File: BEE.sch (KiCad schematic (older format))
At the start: 74 parts, among them J1 RPI1_header, J10 Conn_01x02, J11 Conn_01x02, J12 Conn_01x02, J13 Conn_01x06, J14 Conn_01x03, J15 Conn_02x10_Odd_Even, J16 Conn_01x08, J17 Conn_01x03, J18 Conn_01x03, J19 Conn_01x03, J2 Conn_02x05_Odd_Even, J20 Conn_01x10, J3 Conn_01x03, J4 Conn_01x06, J5 Conn_02x10_Odd_Even, J6 Conn_01x06, J7 Conn_02x10_Odd_Even, J8 Conn_01x08, J9 Conn_01x02, SW1 SW_Push, SW2 SW_Push, SW3 SW_Push, U1 MCP3008, U2 MCP4911, U3 Dip_10xsp3t, U4 Dip_10xsp3t, U5 74AHC595, U6 Display_7Segments

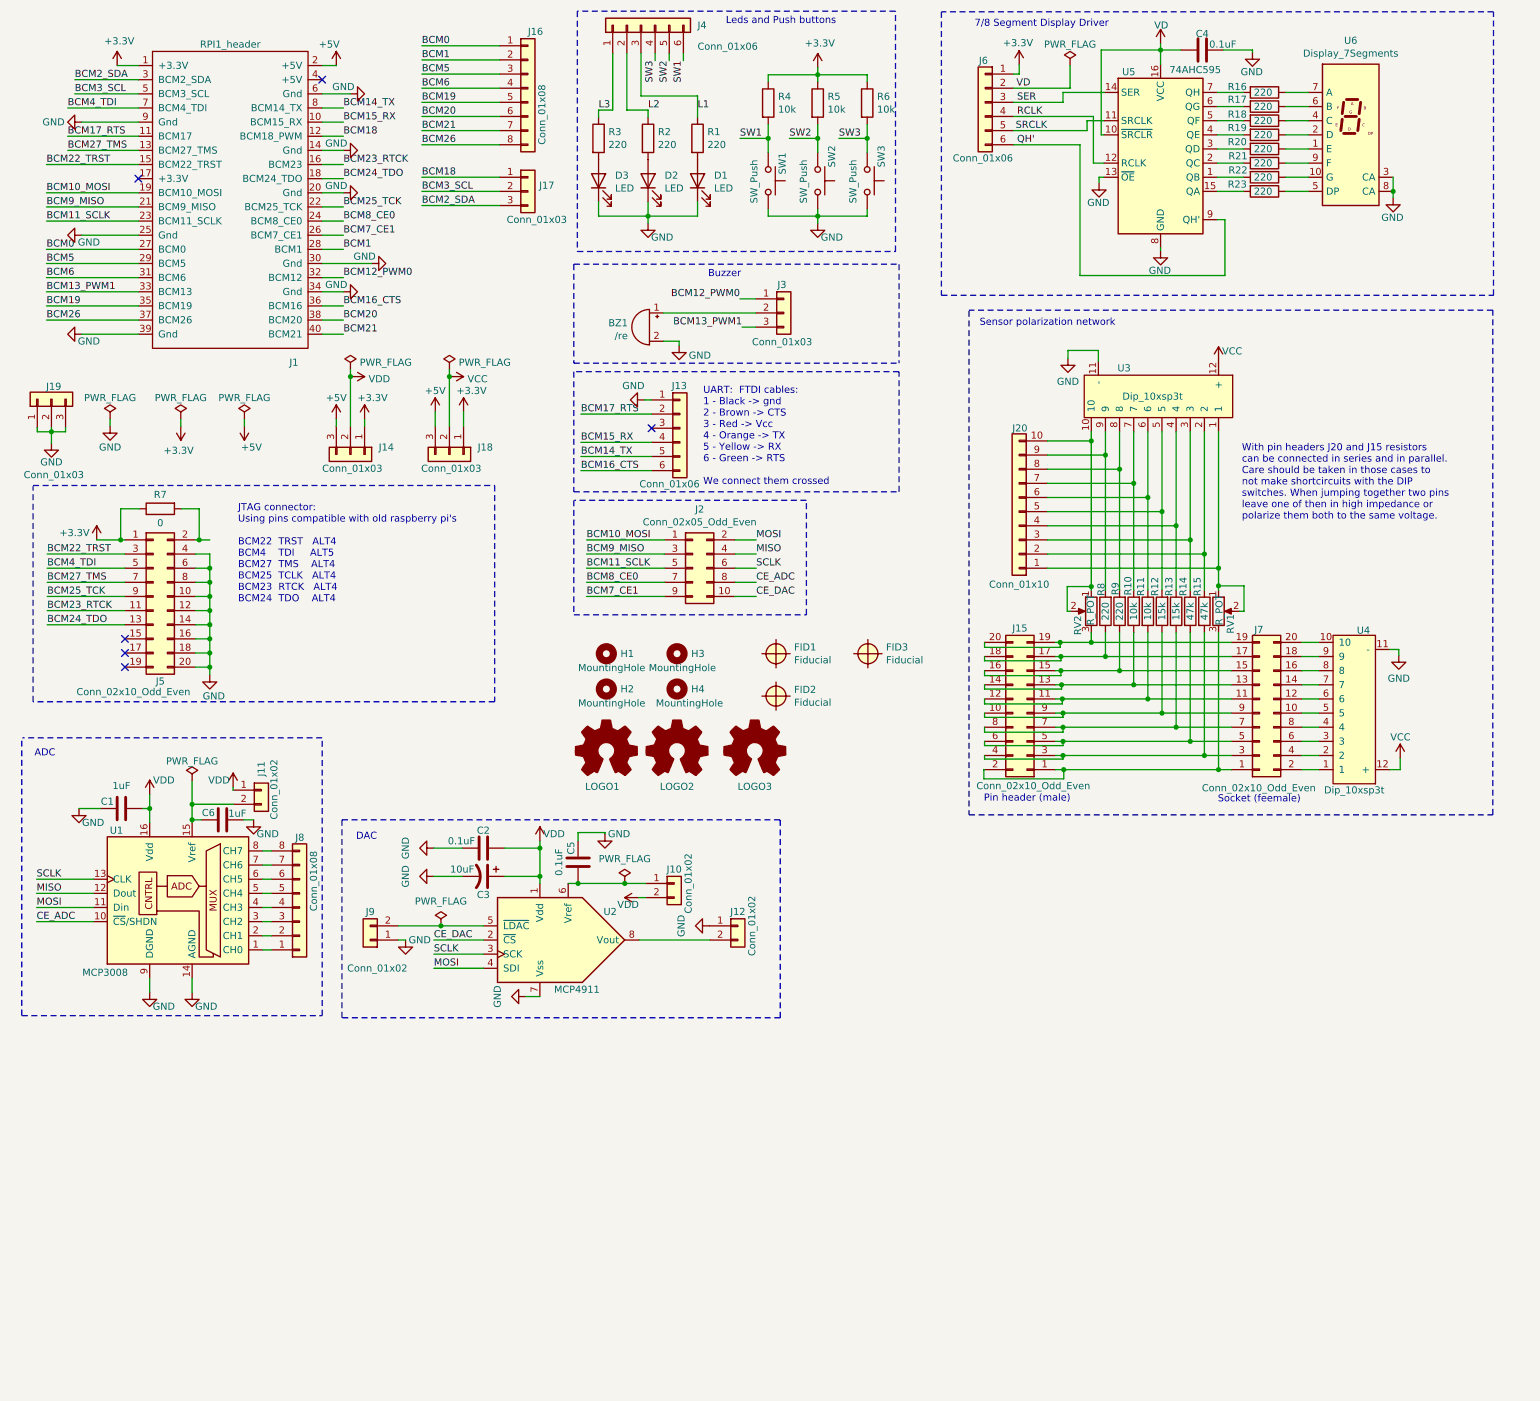
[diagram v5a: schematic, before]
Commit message: RGB Led and J17 adaptation to pimoroni breakouts
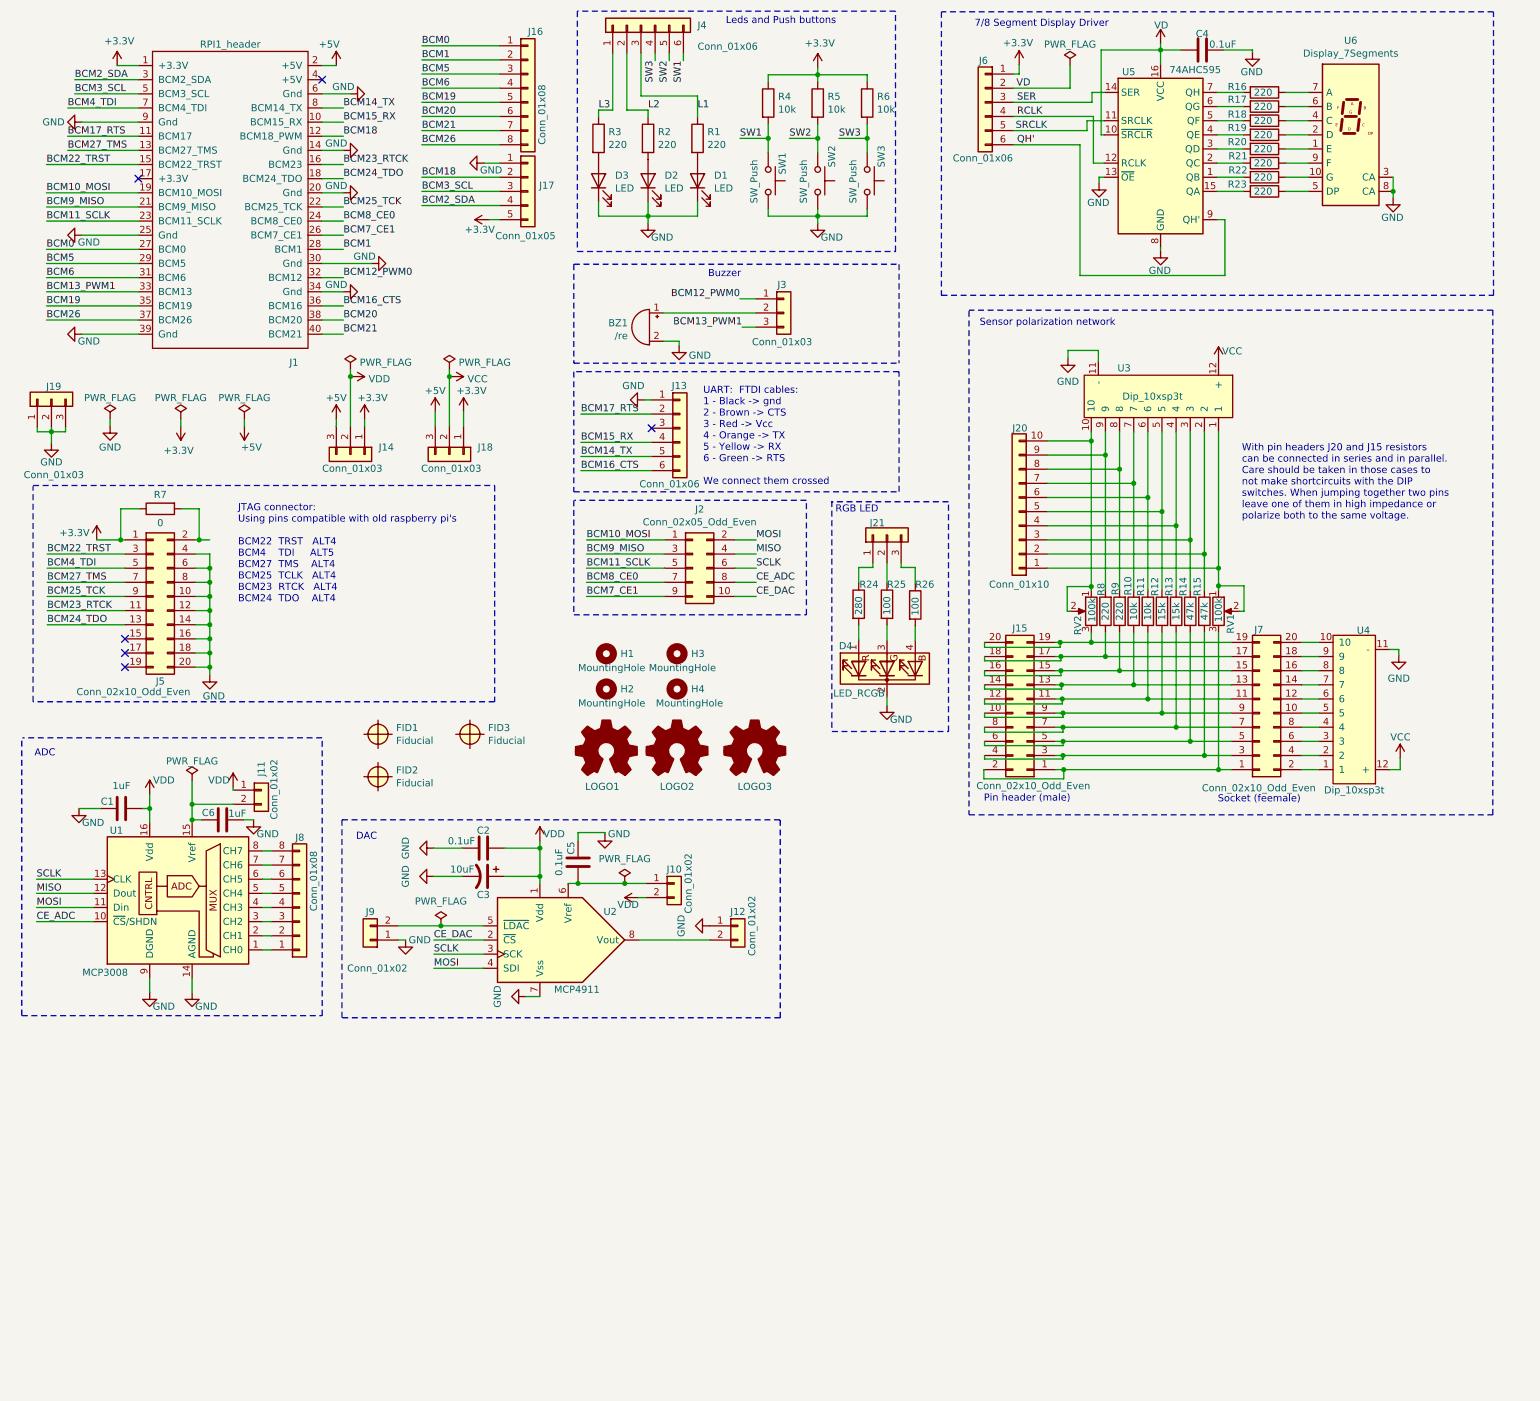
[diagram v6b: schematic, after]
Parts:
- removed J17: Conn_01x03, Connector_PinHeader_2.54mm:PinHeader_1x03_P2.54mm_Vertical, symbol Connector_Generic:Conn_01x03
- added D4: LED_RCGB, BEElib:LED_RCGB, symbol Device:LED_RCGB
- added J17: Conn_01x05, Connector_PinHeader_2.54mm:PinHeader_1x05_P2.54mm_Vertical, symbol Connector_Generic:Conn_01x05
- added J21: Conn_01x03, Connector_PinHeader_2.54mm:PinHeader_1x03_P2.54mm_Vertical, symbol Connector_Generic:Conn_01x03
- added R24: 280, Resistor_SMD:R_0805_2012Metric_Pad1.20x1.40mm_HandSolder, symbol Device:R
- added R25, R26: 100, Resistor_SMD:R_0805_2012Metric_Pad1.20x1.40mm_HandSolder, symbol Device:R
- RV1, RV2: value R_POT -> 100k
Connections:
- net +3V3: now also J17.5 (Pin_5)
- net BCM18: now also J17.2 (Pin_2)
- net BCM2_SDA: now also J17.4 (Pin_4)
- net BCM3_SCL: now also J17.3 (Pin_3)
- net GND: now also D4.2 (K), J17.1 (Pin_1)
- new net: D4.1 (RA), R24.2
- new net: D4.3 (GA), R25.2
- new net: D4.4 (BA), R26.2
- new net: J21.1 (Pin_1), R24.1
- new net: J21.2 (Pin_2), R25.1
- new net: J21.3 (Pin_3), R26.1
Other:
- note added: "RGB LED"
- note added: "With pin headers J20 and J15 resistors\ncan be connected in series and in parallel.\nCare should be taken in those cases to \nnot make shortcircuits with the DIP \nswitches. When jumping together two pins\nleave one of them in high impedance or\npolarize both to the same voltage."
- note removed: "With pin headers J20 and J15 resistors\ncan be connected in series and in parallel.\nCare should be taken in those cases to \nnot make shortcircuits with the DIP \nswitches. When jumping together two pins\nleave one of then in high impedance or\npolarize them both to the same voltage."
- moved on the sheet: FID1, FID2, FID3
